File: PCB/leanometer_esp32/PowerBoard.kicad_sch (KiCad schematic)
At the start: 8 parts, among them J4 VBAT, J5 Conn_01x03, U2 LD1117S33TR_SOT223

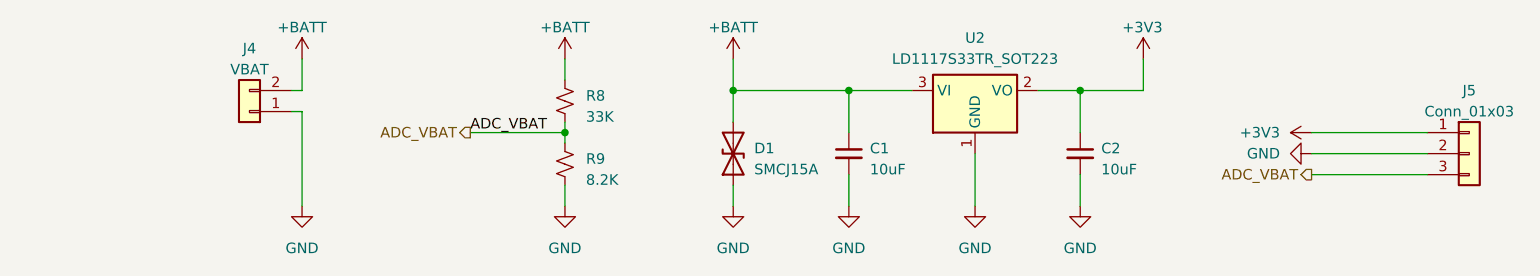
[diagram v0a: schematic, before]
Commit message: Added decoupling cap on ADC_LDR signal
Signed-off-by: theloukou
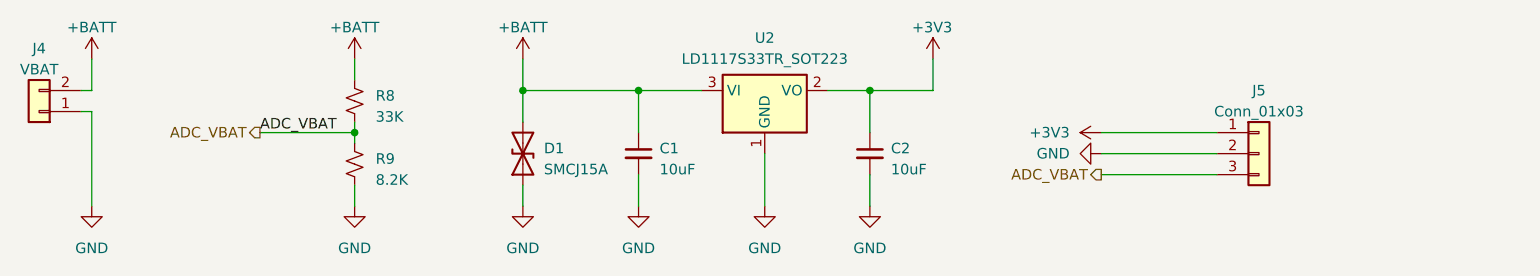
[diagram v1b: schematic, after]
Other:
- moved on the sheet: C1, C2, D1, J4, J5, R8, R9, U2
